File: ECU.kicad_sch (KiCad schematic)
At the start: 0 parts

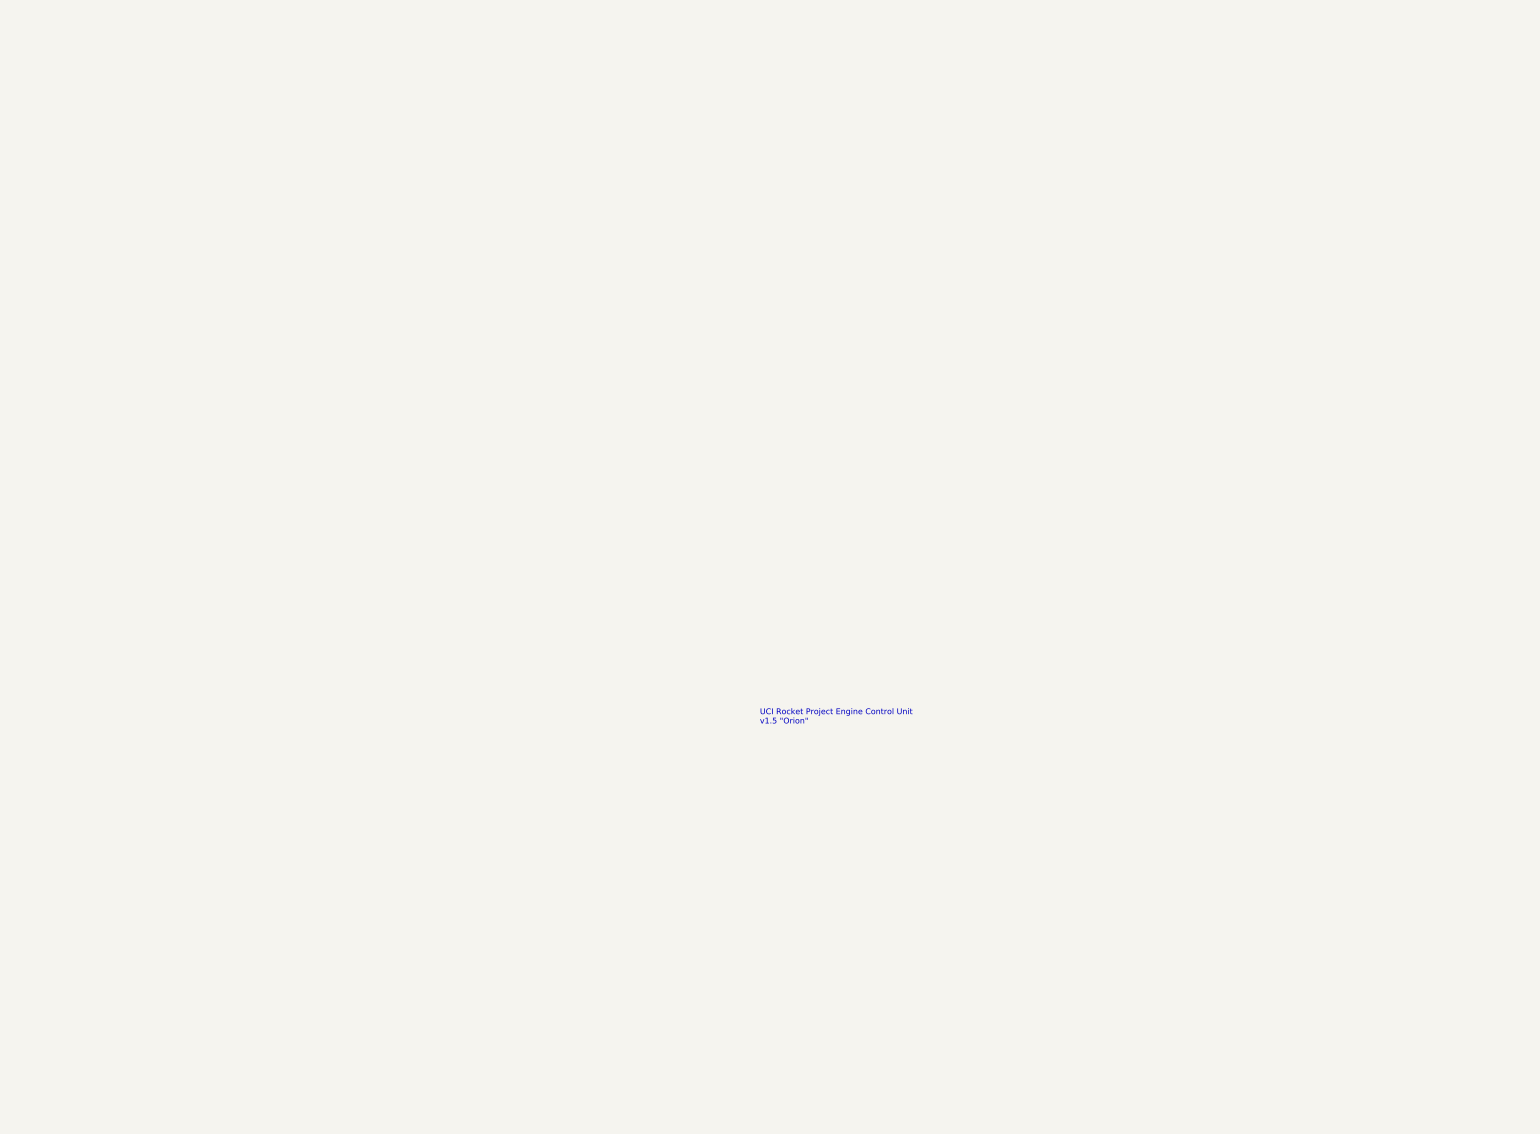
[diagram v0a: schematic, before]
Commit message: Add ucontroller & solenoid switching design
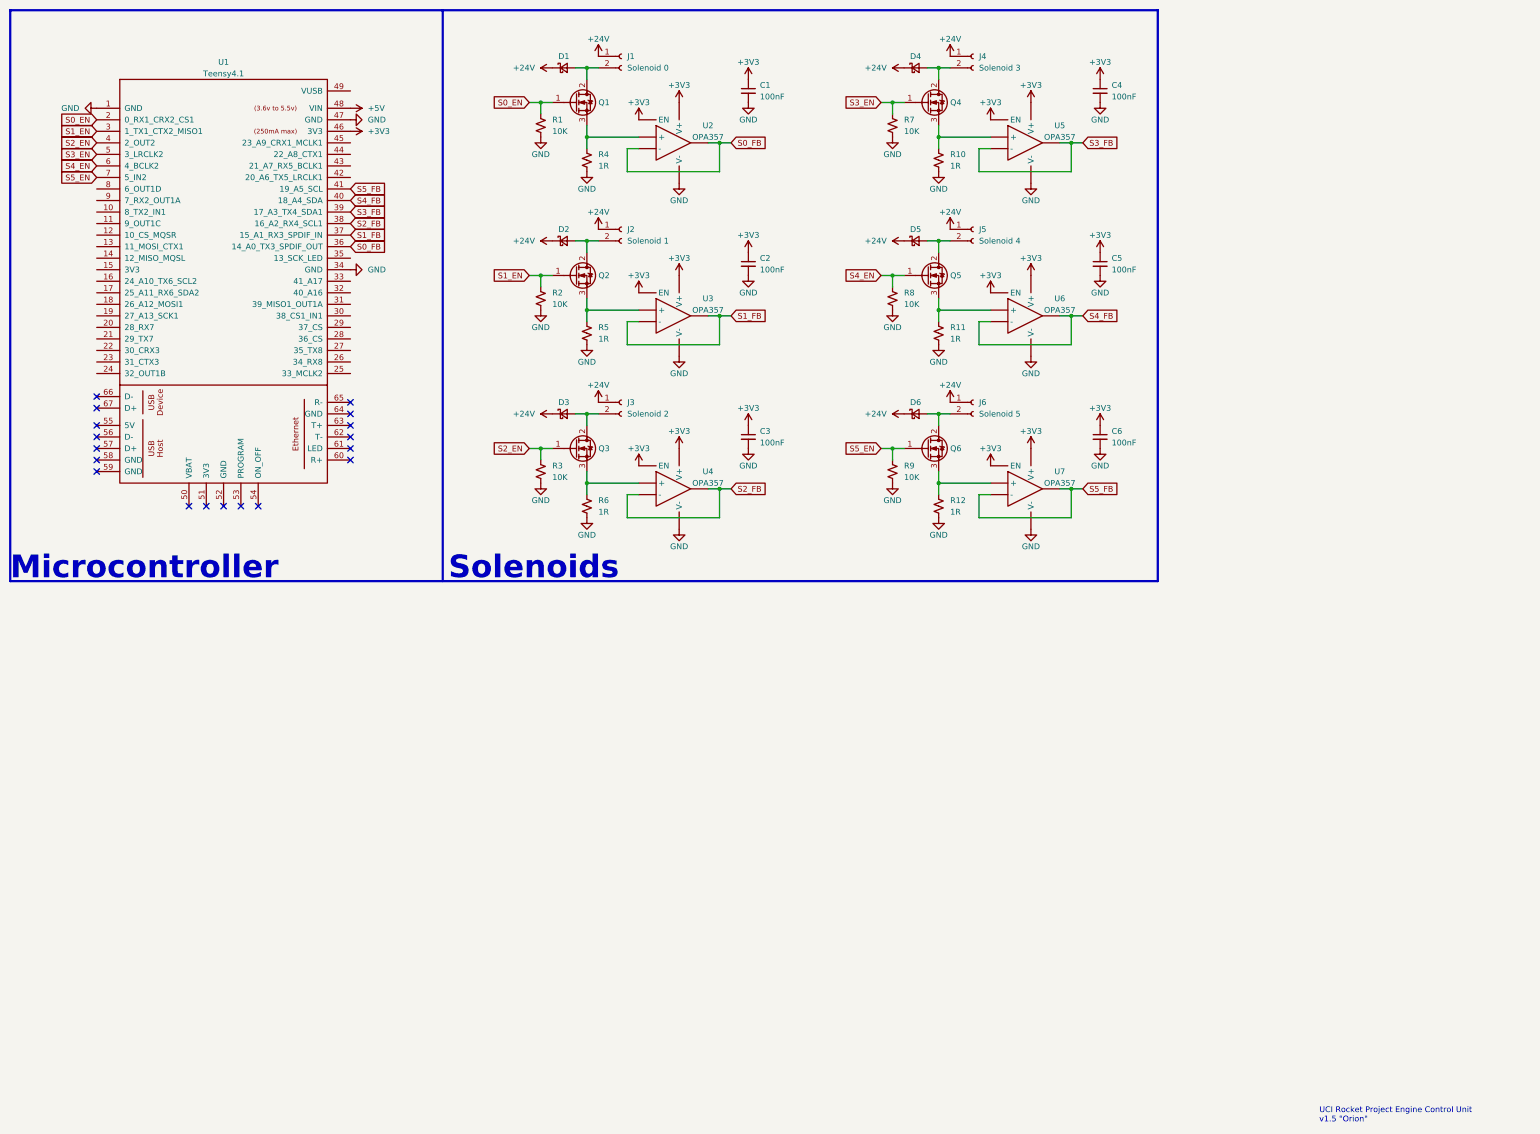
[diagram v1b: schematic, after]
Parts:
- added C1, C2, C3, C4, C5, C6: 100nF, Capacitor_SMD:C_0603_1608Metric, symbol Device:C_Small
- added D1, D2, D3, D4, D5, D6: ~, Diode_SMD:D_SOD-523, symbol Device:D_Schottky_Small
- added J1: Solenoid 0, TerminalBlock:TerminalBlock_bornier-2_P5.08mm, symbol Connector:Conn_01x02_Female
- added J2: Solenoid 1, TerminalBlock:TerminalBlock_bornier-2_P5.08mm, symbol Connector:Conn_01x02_Female
- added J3: Solenoid 2, TerminalBlock:TerminalBlock_bornier-2_P5.08mm, symbol Connector:Conn_01x02_Female
- added J4: Solenoid 3, TerminalBlock:TerminalBlock_bornier-2_P5.08mm, symbol Connector:Conn_01x02_Female
- added J5: Solenoid 4, TerminalBlock:TerminalBlock_bornier-2_P5.08mm, symbol Connector:Conn_01x02_Female
- added J6: Solenoid 5, TerminalBlock:TerminalBlock_bornier-2_P5.08mm, symbol Connector:Conn_01x02_Female
- added Q1, Q2, Q3, Q4, Q5, Q6: ~, Package_TO_SOT_THT:TO-220-3_Vertical, symbol Device:Q_NMOS_GDS
- added R1, R2, R3, R7, R8, R9: 10K, Resistor_SMD:R_0603_1608Metric, symbol Device:R_Small_US
- added R10, R11, R12, R4, R5, R6: 1R, Resistor_SMD:R_0603_1608Metric, symbol Device:R_Small_US
- added U1: Teensy4.1, teensylib:Teensy41, symbol teensy:Teensy4.1
- added U2, U3, U4, U5, U6, U7: OPA357, Package_TO_SOT_SMD:SOT-23-6, symbol ECU:OPA357
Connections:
- new net: Q2.3 (S), R5.1, U3.3 (+)
- new net: D6.2 (A), J6.2 (Pin_2), Q6.2 (D)
- new net: D5.2 (A), J5.2 (Pin_2), Q5.2 (D)
- new net: D4.2 (A), J4.2 (Pin_2), Q4.2 (D)
- new net: D1.2 (A), J1.2 (Pin_2), Q1.2 (D)
- new net: Q1.3 (S), R4.1, U2.3 (+)
- new net: Q5.3 (S), R11.1, U6.3 (+)
- new net: Q3.3 (S), R6.1, U4.3 (+)
- new net: Q4.3 (S), R10.1, U5.3 (+)
- new net: D2.2 (A), J2.2 (Pin_2), Q2.2 (D)
- new net: Q6.3 (S), R12.1, U7.3 (+)
- new net: D3.2 (A), J3.2 (Pin_2), Q3.2 (D)
- new net +24V: D1.1 (K), D2.1 (K), D3.1 (K), D4.1 (K), D5.1 (K), D6.1 (K), J1.1 (Pin_1), J2.1 (Pin_1), J3.1 (Pin_1), J4.1 (Pin_1), J5.1 (Pin_1), J6.1 (Pin_1)
- new net +3V3: C1.1, C2.1, C3.1, C4.1, C5.1, C6.1, U1.46 (3V3), U2.5 (EN), U2.6 (V+), U3.5 (EN), U3.6 (V+), U4.5 (EN), U4.6 (V+), U5.5 (EN), U5.6 (V+), U6.5 (EN), U6.6 (V+), U7.5 (EN), U7.6 (V+)
- new net +5V: U1.48 (VIN)
- new net GND: C1.2, C2.2, C3.2, C4.2, C5.2, C6.2, R1.2, R10.2, R11.2, R12.2, R2.2, R3.2, R4.2, R5.2, R6.2, R7.2, R8.2, R9.2, U1.1 (GND), U1.34 (GND), U1.47 (GND), U2.2 (V-), U3.2 (V-), U4.2 (V-), U5.2 (V-), U6.2 (V-), U7.2 (V-)
- new net S0_EN: Q1.1 (G), R1.1, U1.2 (0_RX1_CRX2_CS1)
- new net S0_FB: U1.36 (14_A0_TX3_SPDIF_OUT), U2.1, U2.4 (-)
- new net S1_EN: Q2.1 (G), R2.1, U1.3 (1_TX1_CTX2_MISO1)
- new net S1_FB: U1.37 (15_A1_RX3_SPDIF_IN), U3.1, U3.4 (-)
- new net S2_EN: Q3.1 (G), R3.1, U1.4 (2_OUT2)
- new net S2_FB: U1.38 (16_A2_RX4_SCL1), U4.1, U4.4 (-)
- new net S3_EN: Q4.1 (G), R7.1, U1.5 (3_LRCLK2)
- new net S3_FB: U1.39 (17_A3_TX4_SDA1), U5.1, U5.4 (-)
- new net S4_EN: Q5.1 (G), R8.1, U1.6 (4_BCLK2)
- new net S4_FB: U1.40 (18_A4_SDA), U6.1, U6.4 (-)
- new net S5_EN: Q6.1 (G), R9.1, U1.7 (5_IN2)
- new net S5_FB: U1.41 (19_A5_SCL), U7.1, U7.4 (-)
- no-connect marks 0 -> 18
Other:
- note added: "Microcontroller"
- note added: "Solenoids"

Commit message: Add thermocouple design
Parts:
- added C10, C7, C8, C9: 100nF, Capacitor_SMD:C_0603_1608Metric, symbol Device:C_Small
- added J10: Thermocouple 3, TerminalBlock:TerminalBlock_bornier-2_P5.08mm, symbol Connector:Conn_01x02_Female
- added J7: Thermocouple 0, TerminalBlock:TerminalBlock_bornier-2_P5.08mm, symbol Connector:Conn_01x02_Female
- added J8: Thermocouple 1, TerminalBlock:TerminalBlock_bornier-2_P5.08mm, symbol Connector:Conn_01x02_Female
- added J9: Thermocouple 2, TerminalBlock:TerminalBlock_bornier-2_P5.08mm, symbol Connector:Conn_01x02_Female
- added U10, U11, U8, U9: MAX31855, Package_SO:SOIC-8_3.9x4.9mm_P1.27mm, symbol ECU:MAX31855
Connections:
- net +3V3: now also C10.1, C7.1, C8.1, C9.1, U10.4 (VCC), U11.4 (VCC), U8.4 (VCC), U9.4 (VCC)
- net GND: now also C10.2, C7.2, C8.2, C9.2, U10.1 (GND), U11.1 (GND), U8.1 (GND), U9.1 (GND)
- net SPI_TC_SCK: now reaches U1.19 (27_A13_SCK1)
- net SPI_TC_SCK: now also U10.5 (SCK), U11.5 (SCK), U8.5 (SCK), U9.5 (SCK)
- net SPI_TC0_~{EN}: now reaches U1.20 (28_RX7)
- net SPI_TC0_~{EN}: now also U8.6 (~{CS})
- net SPI_TC1_~{EN}: now reaches U1.21 (29_TX7)
- net SPI_TC1_~{EN}: now also U9.6 (~{CS})
- net SPI_TC2_~{EN}: now reaches U1.22 (30_CRX3)
- net SPI_TC2_~{EN}: now also U10.6 (~{CS})
- net SPI_TC3_~{EN}: now reaches U1.23 (31_CTX3)
- net SPI_TC3_~{EN}: now also U11.6 (~{CS})
- net SPI_TC_MISO: now reaches U1.31 (39_MISO1_OUT1A)
- net SPI_TC_MISO: now also U10.7 (SO), U11.7 (SO), U8.7 (SO), U9.7 (SO)
- new net: J9.2 (Pin_2), U10.2 (T-)
- new net: J9.1 (Pin_1), U10.3 (T+)
- new net: J7.1 (Pin_1), U8.3 (T+)
- new net: J7.2 (Pin_2), U8.2 (T-)
- new net: J10.1 (Pin_1), U11.3 (T+)
- new net: J10.2 (Pin_2), U11.2 (T-)
- new net: J8.1 (Pin_1), U9.3 (T+)
- new net: J8.2 (Pin_2), U9.2 (T-)
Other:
- note added: "Thermocouples"

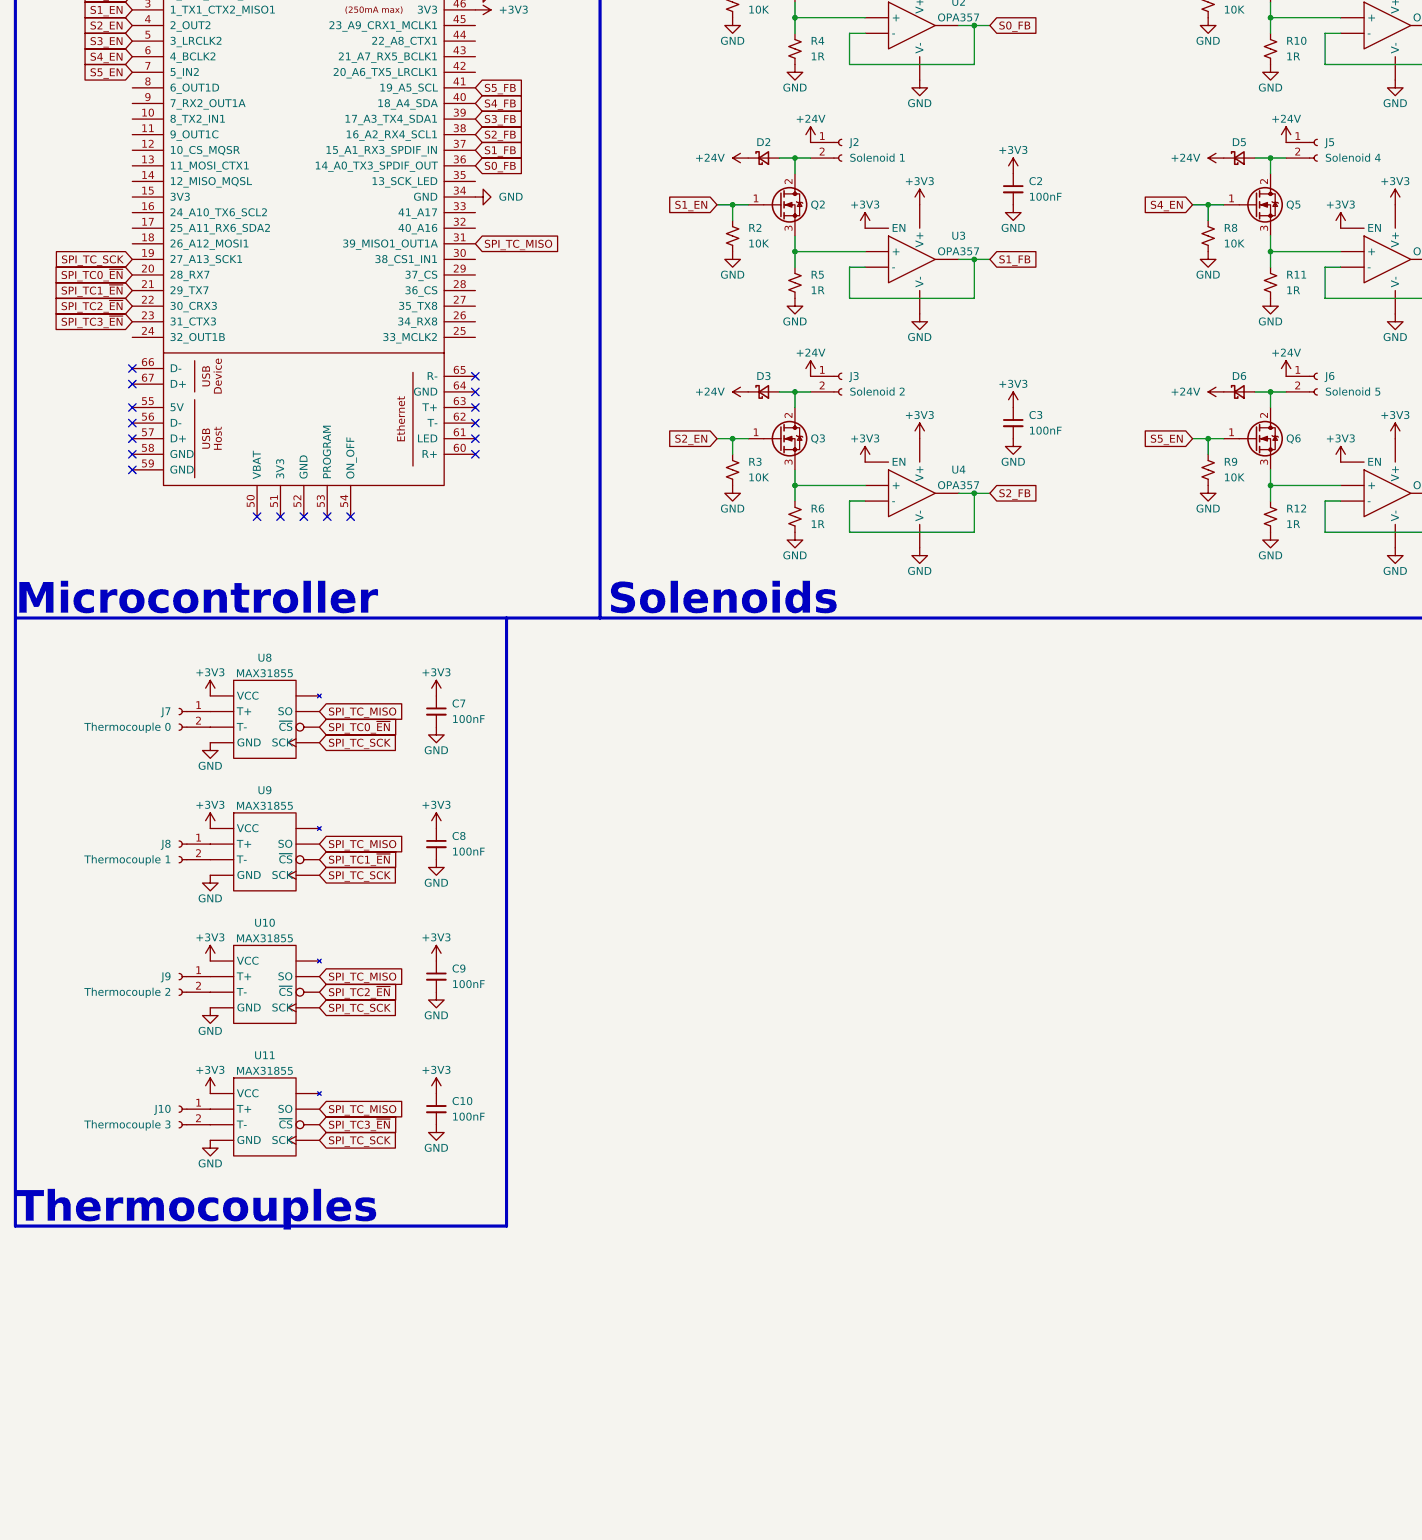
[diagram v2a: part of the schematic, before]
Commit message: Add ethernet & external serial comms ports
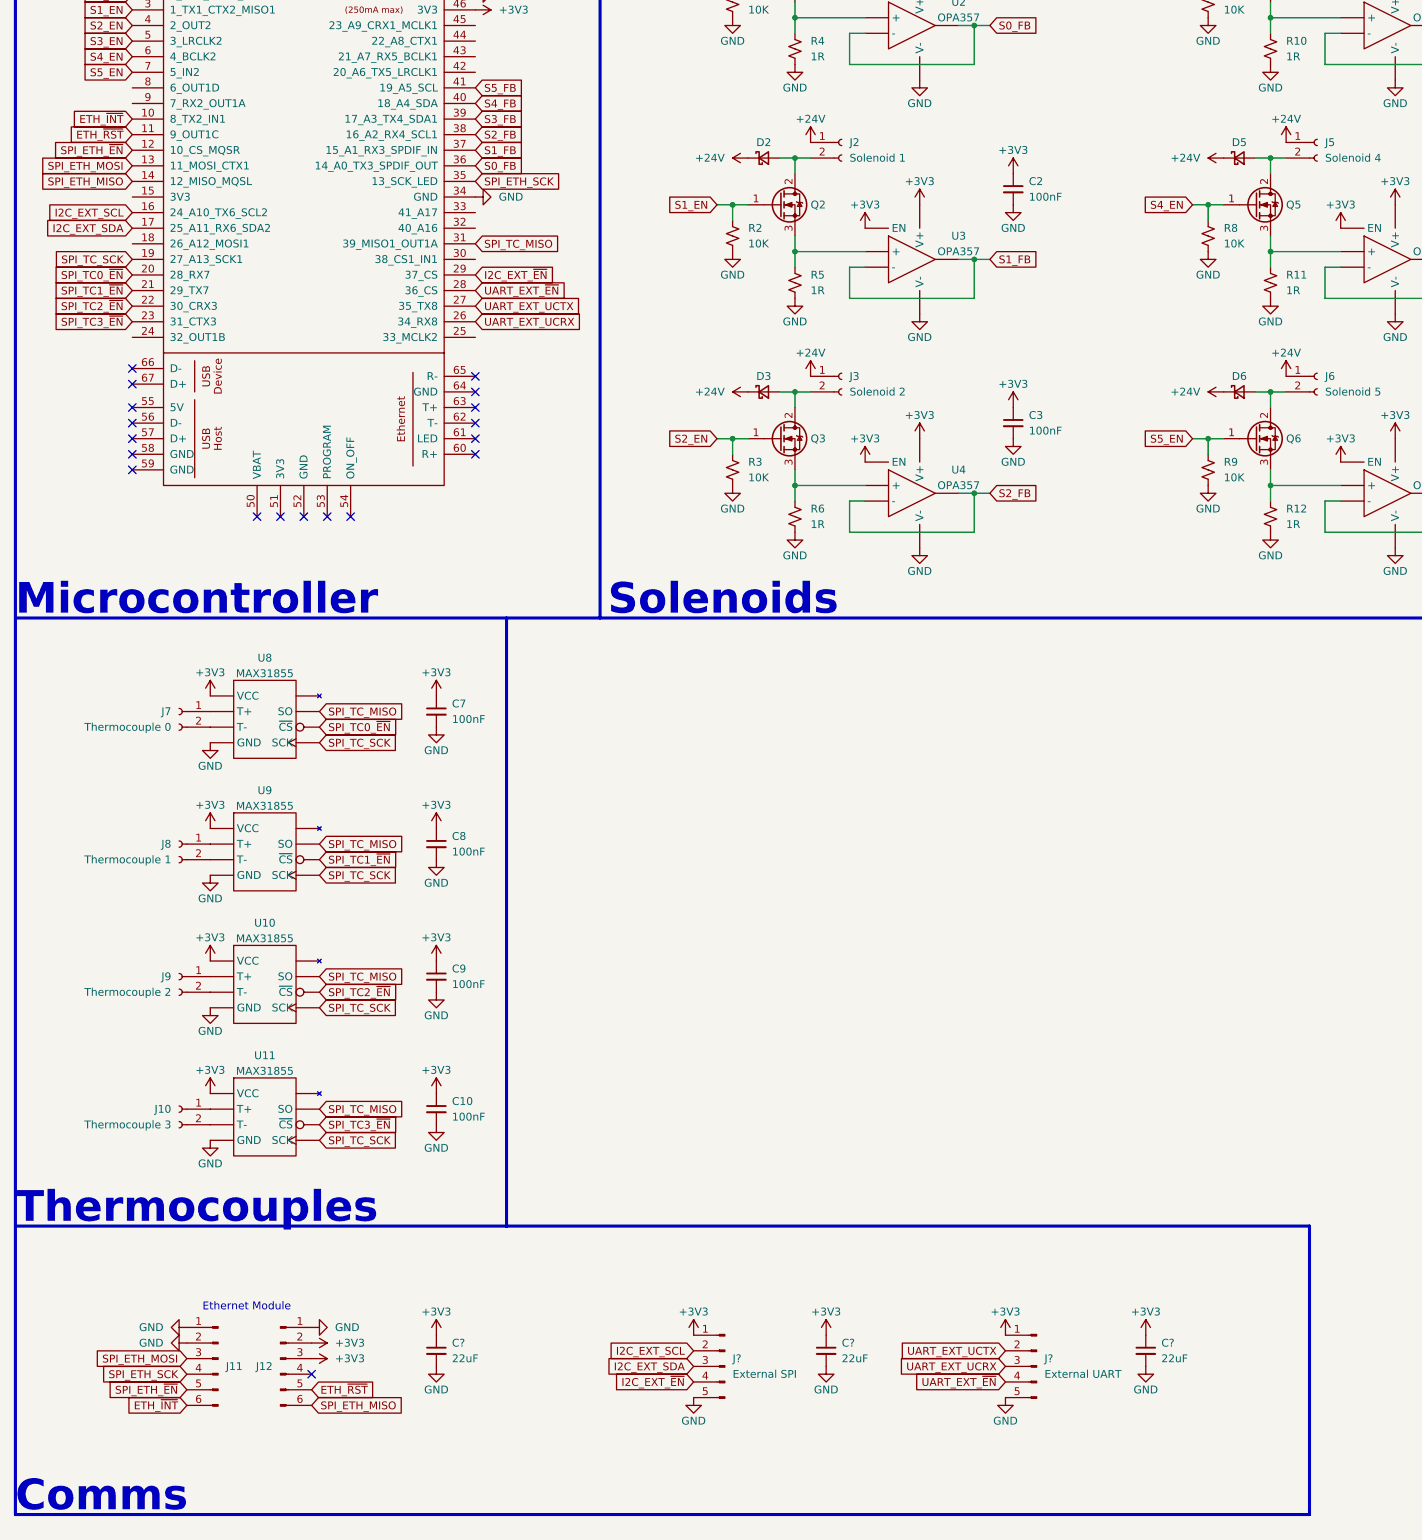
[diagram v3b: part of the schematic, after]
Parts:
- added C? (x3): 22uF, Capacitor_SMD:C_0805_2012Metric, symbol Device:C_Small
- added J11, J12: ~, Connector_PinHeader_2.54mm:PinHeader_1x06_P2.54mm_Vertical, symbol Connector:Conn_01x06_Male
- added J?: External SPI, Connector_PinHeader_2.54mm:PinHeader_1x05_P2.54mm_Vertical, symbol Connector:Conn_01x05_Male
- added J?: External UART, Connector_PinHeader_2.54mm:PinHeader_1x05_P2.54mm_Vertical, symbol Connector:Conn_01x05_Male
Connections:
- net +3V3: now also C?.1, C?.1, C?.1, J12.2 (Pin_2), J12.3 (Pin_3), J?.1 (Pin_1), J?.1 (Pin_1)
- net GND: now also C?.2, C?.2, C?.2, J11.1 (Pin_1), J11.2 (Pin_2), J12.1 (Pin_1), J?.5 (Pin_5), J?.5 (Pin_5)
- net ETH_~{INT}: now reaches U1.10 (8_TX2_IN1)
- net ETH_~{INT}: now also J11.6 (Pin_6)
- net ETH_~{RST}: now reaches U1.11 (9_OUT1C)
- net ETH_~{RST}: now also J12.5 (Pin_5)
- net SPI_ETH_~{EN}: now reaches U1.12 (10_CS_MQSR)
- net SPI_ETH_~{EN}: now also J11.5 (Pin_5)
- net SPI_ETH_MOSI: now reaches U1.13 (11_MOSI_CTX1)
- net SPI_ETH_MOSI: now also J11.3 (Pin_3)
- net SPI_ETH_MISO: now reaches U1.14 (12_MISO_MQSL)
- net SPI_ETH_MISO: now also J12.6 (Pin_6)
- net I2C_EXT_SCL: now reaches U1.16 (24_A10_TX6_SCL2)
- net I2C_EXT_SCL: now also J?.2 (Pin_2)
- net I2C_EXT_SDA: now reaches U1.17 (25_A11_RX6_SDA2)
- net I2C_EXT_SDA: now also J?.3 (Pin_3)
- net UART_EXT_UCRX: now reaches U1.26 (34_RX8)
- net UART_EXT_UCRX: now also J?.3 (Pin_3)
- net UART_EXT_UCTX: now reaches U1.27 (35_TX8)
- net UART_EXT_UCTX: now also J?.2 (Pin_2)
- net UART_EXT_~{EN}: now reaches U1.28 (36_CS)
- net UART_EXT_~{EN}: now also J?.4 (Pin_4)
- net I2C_EXT_~{EN}: now reaches U1.29 (37_CS)
- net I2C_EXT_~{EN}: now also J?.4 (Pin_4)
- net SPI_ETH_SCK: now reaches U1.35 (13_SCK_LED)
- net SPI_ETH_SCK: now also J11.4 (Pin_4)
- no-connect marks 18 -> 19
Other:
- note added: "Comms"
- note added: "Ethernet Module"
